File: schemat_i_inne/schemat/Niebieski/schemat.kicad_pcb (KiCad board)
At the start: 2 copper layers, 195.6 x 86.4 mm, 34 parts, among them J1 Hole1, J2 Hole2, J3 Hole3, J4 Hole4, J5 RJ45, J6 Conn_01x01_Male, J7 Conn_01x01_Male, SW1 SW_DIP_x01, SW2 Left, SW3 Up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

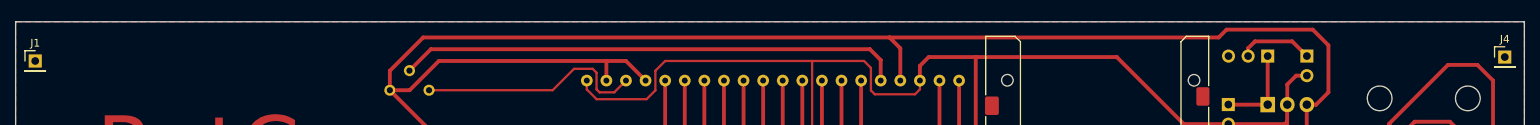
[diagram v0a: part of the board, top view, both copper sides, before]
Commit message: Bardzo drobna zmiana plytki
-> Wyrownano dw gorne skrajne otwory
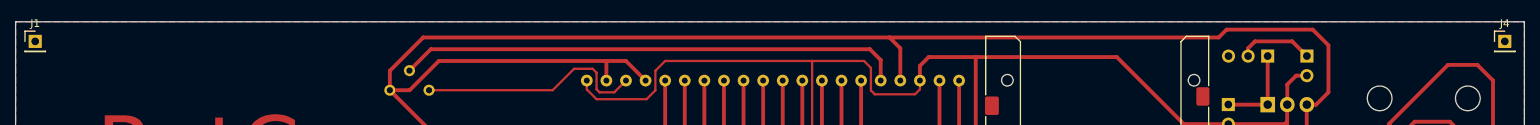
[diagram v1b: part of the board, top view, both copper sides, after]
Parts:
- moved J1 2.54 mm to (48.3, 55.9)
- moved J4 2.03 mm to (238.8, 55.9)
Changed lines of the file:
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@@
   )
   (footprint "Connector_PinHeader_2.54mm:PinHeader_1x01_P2.54mm_Vertical" (layer "F.Cu")
-    (at 48.26 58.42)
+    (at 48.26 55.88)
     (descr "Through hole straight pin header, 1x01, 2.54mm pitch, single row")
     (tags "Through hole pin header THT 1x01 2.54mm single row")
@@
   )
   (footprint "Connector_PinHeader_2.54mm:PinHeader_1x01_P2.54mm_Vertical" (layer "F.Cu")
-    (at 238.76 57.912)
+    (at 238.76 55.88)
     (descr "Through hole straight pin header, 1x01, 2.54mm pitch, single row")
     (tags "Through hole pin header THT 1x01 2.54mm single row")
@@
   (segment (start 167.209 97.105) (end 165.608 95.504) (width 0.5) (layer "F.Cu") (net 40))
   (segment (start 231.4295 75.1485) (end 231.4295 74.8945) (width 0.5) (layer "F.Cu") (net 40))
-  (segment (start 166.497 104.648) (end 149.098 104.648) (width 0.5) (layer "F.Cu") (net 41))
   (segment (start 166.497 104.648) (end 171.577 99.568) (width 0.5) (layer "F.Cu") (net 41))
   (segment (start 205.414 102.986) (end 205.414 101.966) (width 0.5) (layer "F.Cu") (net 41))
   (segment (start 146.350517 104.648) (end 149.098 104.648) (width 0.3) (layer "F.Cu") (net 41))
   (segment (start 145.77215 104.069633) (end 146.350517 104.648) (width 0.3) (layer "F.Cu") (net 41))
+  (segment (start 166.497 104.648) (end 149.098 104.648) (width 0.5) (layer "F.Cu") (net 41))
   (segment (start 141.975767 100.27325) (end 145.77215 104.069633) (width 0.3) (layer "F.Cu") (net 41))
   (segment (start 205.414 100.706) (end 205.414 101.966) (width 0.5) (layer "F.Cu") (net 41))

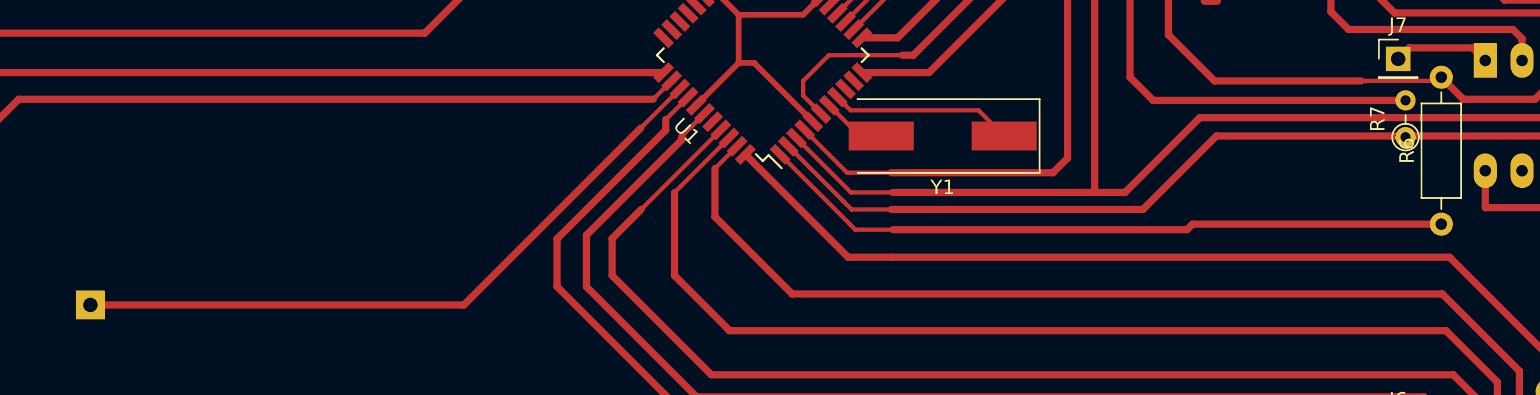
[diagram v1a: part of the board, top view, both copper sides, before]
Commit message: Updated PCB ->key isn't anymore on PB4
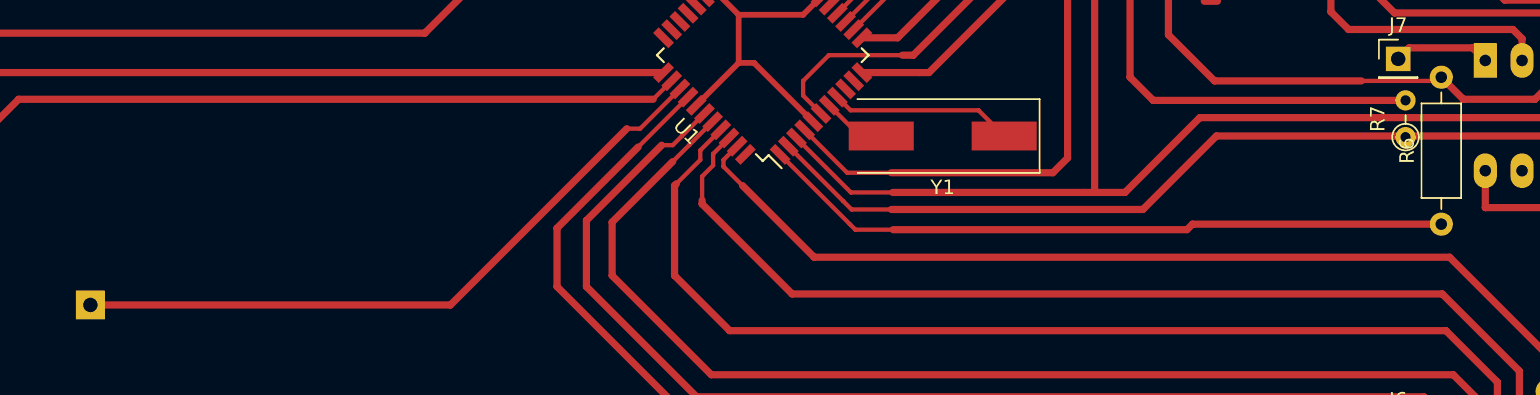
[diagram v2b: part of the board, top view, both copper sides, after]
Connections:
- U1 pad 40: unconnected-(U1-Pad40) -> Net-(SW4-Pad1)
- U1 pad 41: Net-(SW4-Pad1) -> Net-(SW5-Pad1)
- U1 pad 42: Net-(SW5-Pad1) -> Net-(SW3-Pad1)
- U1 pad 43: Net-(SW3-Pad1) -> Net-(SW2-Pad1)
- U1 pad 44: Net-(SW2-Pad1) -> unconnected-(U1-Pad44)
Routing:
- net Net-(SW2-Pad1): track 76.5 -> 79.5 mm
- net Net-(SW3-Pad1): track 105.2 -> 106.3 mm

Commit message: new version of schema and board
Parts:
- removed J7: Conn_01x01_Male, Connector_PinHeader_2.54mm:PinHeader_1x01_P2.54mm_Vertical
- removed R6: 0R, Resistor_THT:R_Axial_DIN0207_L6.3mm_D2.5mm_P10.16mm_Horizontal
- removed R7: 0R, Resistor_THT:R_Axial_DIN0204_L3.6mm_D1.6mm_P2.54mm_Vertical
- added C5: 100N, Capacitor_SMD:C_0805_2012Metric, B.Cu at (172.7, 72.4)
- added D1: D, Diode_SMD:D_0201_0603Metric, B.Cu at (218.4, 89.1)
- added L1: 10uH, Inductor_SMD:L_6.3x6.3_H3, B.Cu at (179.1, 67.3)
- added U7: ~, joystick:joystickTHT, F.Cu at (111.8, 71.1)
- added U8: ~, joystick:joystickTHT, F.Cu at (215.9, 71.1)
- BT1: footprint Connector_PinHeader_2.54mm:PinHeader_1x02_P2.54mm_Vertical -> Connector_PinSocket_2.54mm:PinSocket_1x02_P2.54mm_Vertical
- C1, C2, C3: footprint Connector_PinHeader_2.54mm:PinHeader_1x02_P2.54mm_Vertical -> Capacitor_SMD:C_0805_2012Metric
- C4: footprint Connector_PinHeader_2.54mm:PinHeader_1x02_P2.54mm_Vertical -> Capacitor_SMD:CP_Elec_6.3x5.4_Nichicon
- J5: value RJ45 -> programming port; footprint Connector_RJ:RJ45_Amphenol_54602-x08_Horizontal -> Connector_PinSocket_2.54mm:PinSocket_1x06_P2.54mm_Vertical; moved to F.Cu
- J6: value Conn_01x01_Male -> USB_B_Micro; footprint Connector_PinHeader_2.54mm:PinHeader_1x01_P2.54mm_Vertical -> Connector_USB:USB_Micro-AB_Molex_47590-0001; moved to B.Cu
- R1, R2, R3, R4, U4, U6, Y1: moved to B.Cu
- SW1: footprint Connector_PinHeader_2.54mm:PinHeader_1x03_P2.54mm_Vertical -> Button_Switch_SMD:SW_DIP_SPSTx01_Slide_Copal_CVS-01xB_W5.9mm_P1mm
- SW2: value Left -> Home; footprint Button_Switch_THT:SW_PUSH-12mm -> Button_Switch_SMD:SW_Push_1P1T_NO_6x6mm_H9.5mm; moved to F.Cu
- SW3: value Up -> triggerR; footprint Button_Switch_THT:SW_PUSH-12mm -> Button_Switch_THT:SW_Tactile_SPST_Angled_PTS645Vx31-2LFS
- SW4: value Down -> Select; footprint Button_Switch_THT:SW_PUSH-12mm -> Button_Switch_SMD:SW_Push_1P1T_NO_6x6mm_H9.5mm; moved to F.Cu
- SW5: value Right -> triggerL; footprint Button_Switch_THT:SW_PUSH-12mm -> Button_Switch_THT:SW_Tactile_SPST_Angled_PTS645Vx31-2LFS
- SW6: value Jump -> BumperL; footprint Button_Switch_THT:SW_PUSH-12mm -> Button_Switch_THT:SW_Tactile_SPST_Angled_PTS645Vx31-2LFS; moved to F.Cu
- SW7: value Punch -> BumperR; footprint Button_Switch_THT:SW_PUSH-12mm -> Button_Switch_THT:SW_Tactile_SPST_Angled_PTS645Vx31-2LFS; moved to F.Cu
- U1: value ATmega32A-AU -> ATmega1284P; moved to B.Cu
- U2: footprint Package_TO_SOT_THT:TO-220-3_Vertical -> Package_TO_SOT_SMD:TO-252-2
- U3: moved to F.Cu
- U5: footprint Package_DIP:DIP-14_W7.62mm_LongPads -> Package_SO:SO-14_3.9x8.65mm_P1.27mm
- moved J1 158.9 mm to (207.0, 62.2)
- moved SW6 149.2 mm to (207.6, 53.3), turned to 0 degrees
- moved SW5 141.9 mm to (110.2, 53.3)
- moved J3 120.0 mm to (120.7, 115.6)
- moved RV1 115.6 mm to (214.9, 61.0), turned to 180 degrees
- moved J2 104.2 mm to (120.7, 62.2)
- moved J5 102.5 mm to (121.9, 81.3), turned to 180 degrees
- moved SW2 95.7 mm to (112.9, 104.4), turned to 0 degrees
- moved SW7 83.3 mm to (115.8, 53.3), turned to 0 degrees
- moved J4 67.6 mm to (207.0, 115.6)
- moved C4 61.9 mm to (161.5, 107.2), turned to 90 degrees
- moved R1 57.0 mm to (154.9, 73.7), turned to -90 degrees
- moved U6 53.0 mm to (141.7, 101.4)
- moved SW3 52.6 mm to (222.0, 53.3)
- moved R4 48.3 mm to (143.8, 85.9), turned to 0 degrees
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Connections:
- BZ1 pad 1: Net-(BZ1-Pad1) -> Net-(BZ1--)
- C1 pad 1: Net-(C1-Pad1) -> Net-(D1-K)
- J5 pad 1: +5V -> /MOSI
- J5 pad 2: GND -> /MISO
- J5 pad 3: unconnected-(J5-Pad3) -> /SCK
- J5 pad 4: Net-(J5-Pad4) -> Net-(J5-Pin_4)
- J5 pad 5: Net-(J5-Pad5) -> +5V
- J5 pad 6: /SCK -> GND
- J6 pad 1: /CS -> +5V
- SW1 pad 1: Net-(C1-Pad1) -> Net-(D1-A)
- SW2 pad 1: Net-(SW2-Pad1) -> +5V
- SW2 pad 2: GND -> Net-(U1-PD0)
- SW3 pad 1: Net-(SW3-Pad1) -> +5V
- SW3 pad 2: GND -> Net-(U1-PA5)
- SW4 pad 1: Net-(SW4-Pad1) -> +5V
- SW4 pad 2: GND -> Net-(U1-PB2)
- SW5 pad 1: Net-(SW5-Pad1) -> Net-(U1-PD2)
- SW5 pad 2: GND -> +5V
- SW6 pad 1: Net-(SW6-Pad1) -> Net-(U1-PA4)
- SW6 pad 2: GND -> +5V
- SW7 pad 1: Net-(SW7-Pad1) -> +5V
- SW7 pad 2: GND -> Net-(U1-PD1)
- U1 pad 10: unconnected-(U1-Pad10) -> Net-(U1-PD1)
- U1 pad 11: Net-(J5-Pad4) -> Net-(U1-PD2)
- U1 pad 27: +5V -> Net-(U1-AVCC)
- U1 pad 29: unconnected-(U1-Pad29) -> Net-(U1-AREF)
- U1 pad 32: unconnected-(U1-Pad32) -> Net-(U1-PA5)
- U1 pad 33: unconnected-(U1-Pad33) -> Net-(U1-PA4)
- U1 pad 34: Net-(SW7-Pad1) -> Net-(U1-PA3)
- U1 pad 35: Net-(SW6-Pad1) -> Net-(U1-PA2)
- U1 pad 36: Net-(BZ1-Pad1) -> Net-(U1-PA1)
- U1 pad 37: /CS -> Net-(U1-PA0)
- U1 pad 4: Net-(J5-Pad5) -> Net-(J5-Pin_4)
- U1 pad 40: Net-(SW4-Pad1) -> unconnected-(U1-PB0-Pad40)
- U1 pad 41: Net-(SW5-Pad1) -> unconnected-(U1-PB1-Pad41)
- U1 pad 42: Net-(SW3-Pad1) -> Net-(U1-PB2)
- U1 pad 43: Net-(SW2-Pad1) -> Net-(BZ1--)
- U1 pad 44: unconnected-(U1-Pad44) -> /CS
- U1 pad 9: unconnected-(U1-Pad9) -> Net-(U1-PD0)
- U2 pad 1: Net-(C1-Pad1) -> Net-(D1-K)
- U5 pad 1: Net-(J7-Pad1) -> /CS
- U5 pad 3: Net-(J5-Pad8) -> /MOSI
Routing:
- net GND: track 908.8 -> 57.6 mm
- net +5V: track 425.4 -> 23.9 mm
- net /SCK: track 154.3 -> 20.3 mm
- net Net-(SW5-Pad1): track 121.6 -> 0.00 mm
- net Net-(SW4-Pad1): track 118.9 -> 0.00 mm
- net Net-(J5-Pad5): track 111.2 -> 0.00 mm
- net Net-(J5-Pad8): track 109.6 -> 0.00 mm
- net Net-(U1-PA1): track 0.00 -> 107.0 mm
- net Net-(SW3-Pad1): track 106.3 -> 0.00 mm
- net Net-(J5-Pad7): track 104.0 -> 0.00 mm
- net Net-(SW6-Pad1): track 93.9 -> 0.00 mm
- net Net-(SW7-Pad1): track 92.7 -> 0.00 mm
- net Net-(J5-Pad4): track 90.1 -> 0.00 mm
- net Net-(U1-PA0): track 0.00 -> 85.9 mm
- net Net-(SW2-Pad1): track 79.5 -> 0.00 mm
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- removed copper zone on F.Cu, net GND
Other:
- board size 195.6 x 86.4 mm -> 121.4 x 70.4 mm
- board text added: "Battery"
- board text removed: "RetCon by KK"
- board text removed: "optional- if needed"

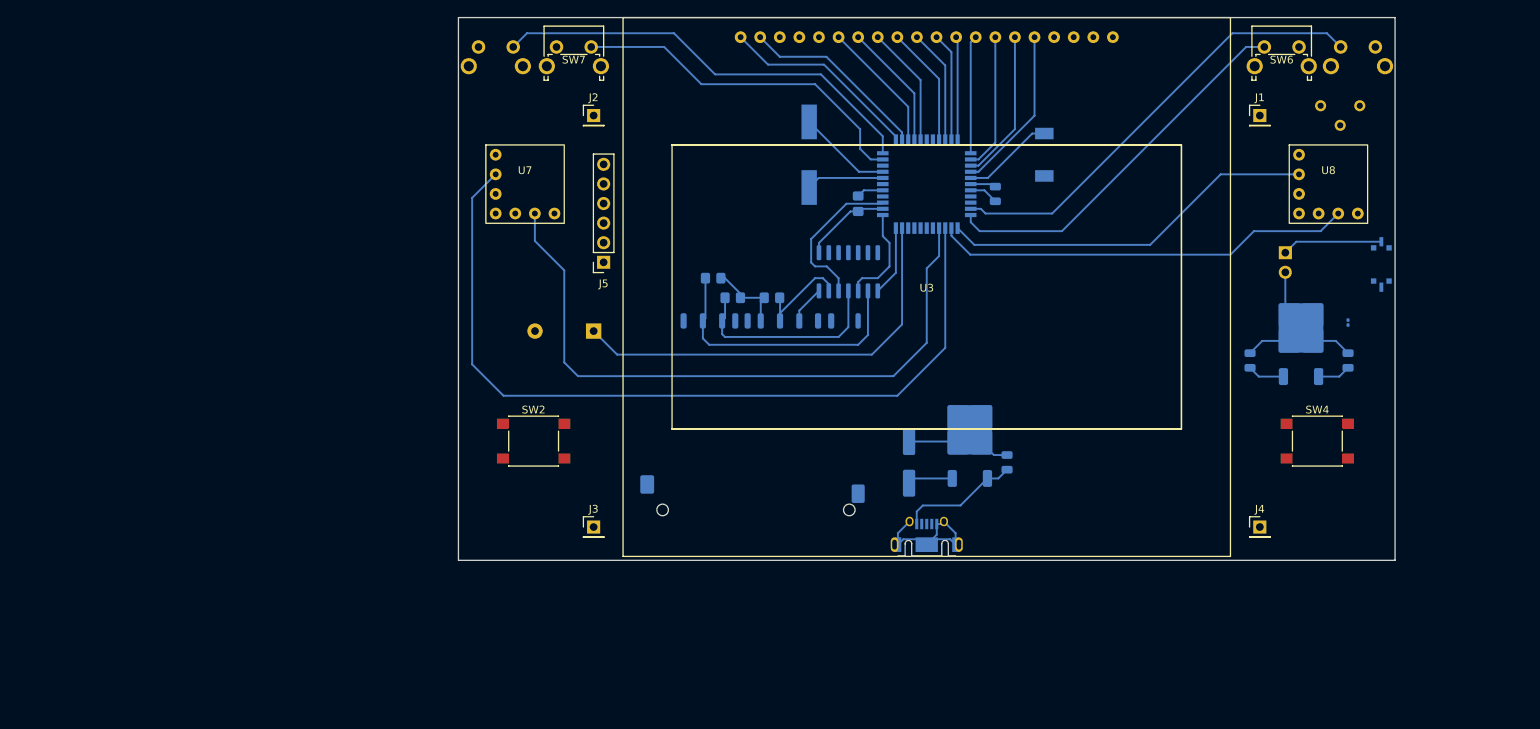
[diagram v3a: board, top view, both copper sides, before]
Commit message: Complete board, DRC test passed
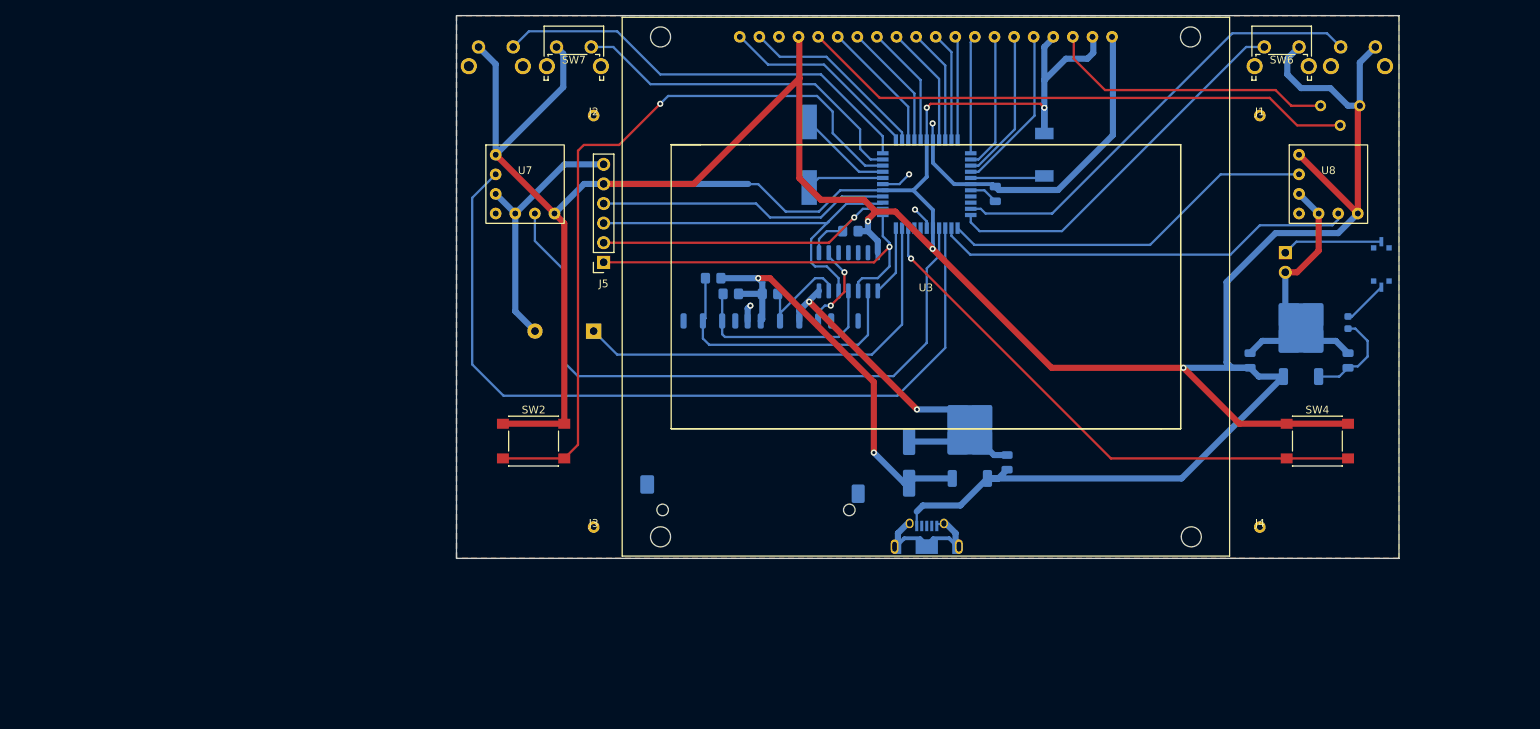
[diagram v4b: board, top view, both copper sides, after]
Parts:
- D1: footprint Diode_SMD:D_0201_0603Metric -> Diode_SMD:D_0603_1608Metric
- J1: value Hole1 -> ~; footprint Connector_PinHeader_2.54mm:PinHeader_1x01_P2.54mm_Vertical -> Holes:One_hole
- J2: value Hole2 -> ~; footprint Connector_PinHeader_2.54mm:PinHeader_1x01_P2.54mm_Vertical -> Holes:One_hole
- J3: value Hole3 -> ~; footprint Connector_PinHeader_2.54mm:PinHeader_1x01_P2.54mm_Vertical -> Holes:One_hole
- J4: value Hole4 -> ~; footprint Connector_PinHeader_2.54mm:PinHeader_1x01_P2.54mm_Vertical -> Holes:One_hole
- J6: footprint Connector_USB:USB_Micro-AB_Molex_47590-0001 -> USB:microUSB
- moved R1 3.70 mm to (153.9, 77.2), turned to 180 degrees
- moved R4 0.57 mm to (143.5, 85.3)
- moved R3 0.57 mm to (138.4, 85.3)
- moved J6 0.25 mm to (163.8, 118.1)
- moved U3 0.12 mm to (163.7, 84.5)
- turned L1 to -90 degrees
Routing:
- net +5V: track 23.9 -> 489.4 mm, vias 0 -> 5
- net GND: track 57.6 -> 181.5 mm, vias 0 -> 6
- net Net-(U1-PD0): track 0.00 -> 96.4 mm, vias 0 -> 1
- net Net-(U3-V0): track 0.00 -> 72.3 mm
- net Net-(U1-PB2): track 0.00 -> 71.5 mm, vias 0 -> 1
- net +3V3: track 16.0 -> 55.5 mm, vias 0 -> 2
- net Net-(J5-Pin_4): track 0.00 -> 38.1 mm
- net /MOSI: track 13.1 -> 51.0 mm, vias 0 -> 1
- net Net-(U3-VEE): track 0.00 -> 37.3 mm
- net /MISO: track 11.4 -> 45.7 mm, vias 0 -> 1
- net /SCK: track 20.3 -> 49.6 mm
- net Net-(U6-DAT0): track 0.00 -> 11.5 mm, vias 0 -> 2
- net Net-(D1-K): track 4.29 -> 12.7 mm
- net Net-(D1-A): track 0.00 -> 5.89 mm
- net Net-(U1-AVCC): track 11.9 -> 9.65 mm
- added copper zone on B.Cu, net GND
- added copper zone on F.Cu, net GND
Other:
- board size 121.4 x 70.4 mm -> 122.2 x 70.4 mm
- rule pad_to_mask_clearance: 0.051 -> 0
